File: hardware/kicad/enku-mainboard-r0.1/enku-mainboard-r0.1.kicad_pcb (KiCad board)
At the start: 4 copper layers, 54 x 94 mm, 124 parts, among them U1 ESP32-S3-WROOM-1-N16R8

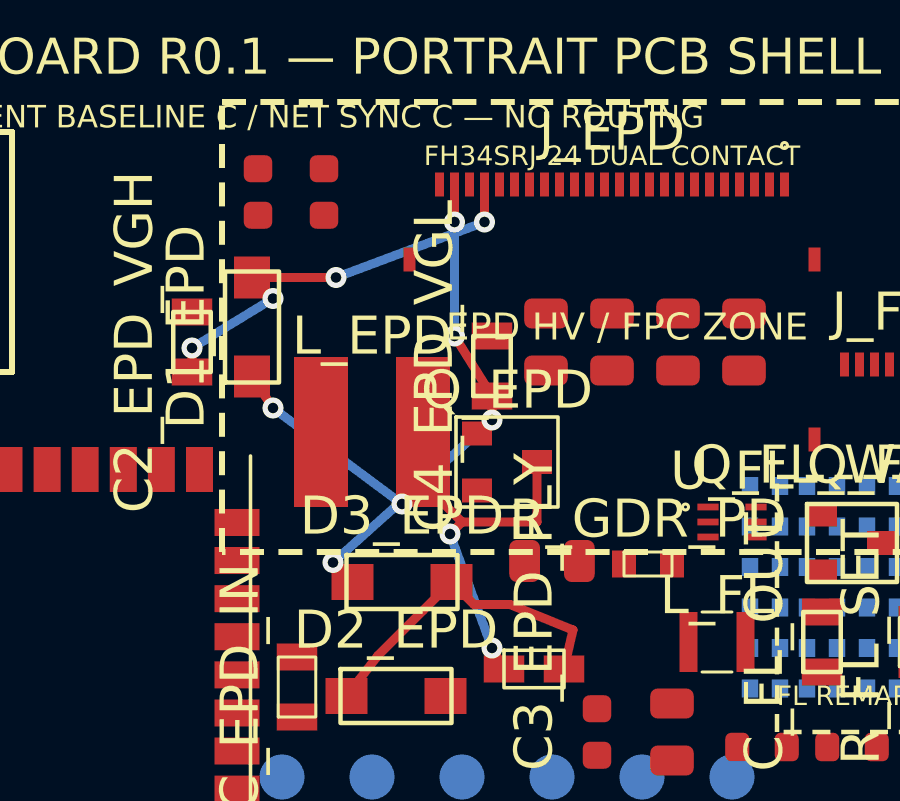
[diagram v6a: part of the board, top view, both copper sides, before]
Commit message: Reroute EPD VGL around proven HV paths
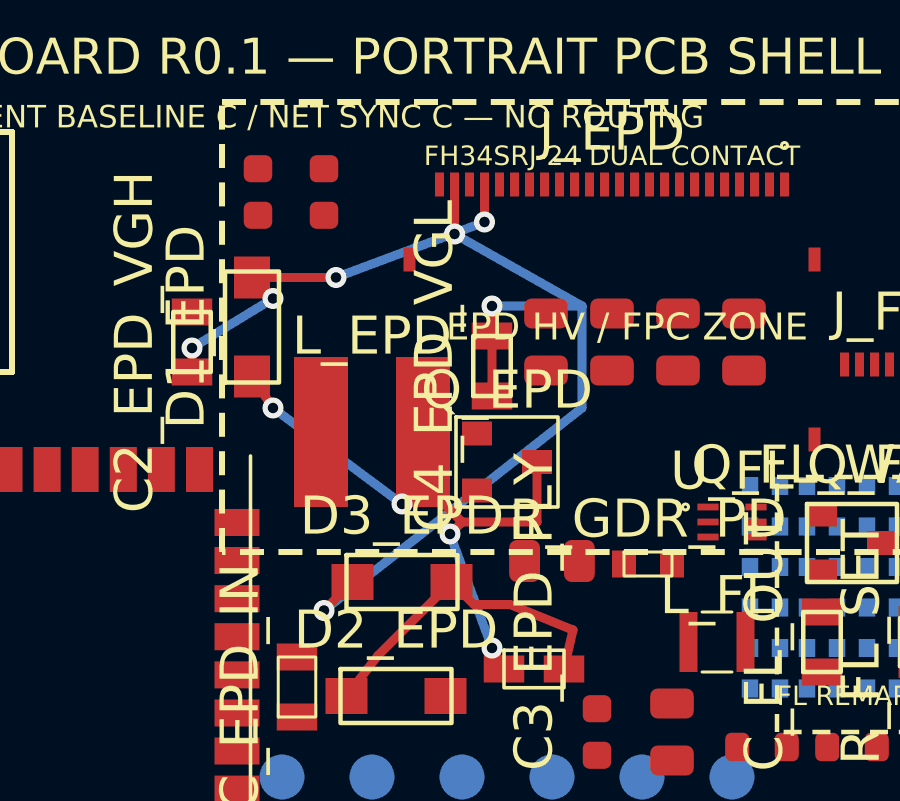
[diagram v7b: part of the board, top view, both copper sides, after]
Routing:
- net EPD_VGL: track 16.2 -> 28.2 mm, vias 4 -> 3
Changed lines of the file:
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@@
   (via (at 44.0 32.2) (size 0.7) (drill 0.35) (layers "F.Cu" "B.Cu") (net 26))
   (segment (start 44.0 32.2) (end 44.0 33.0) (width 0.3) (layer "F.Cu") (net 26))
-  (segment (start 49.35 40.0) (end 48.7 39.35) (width 0.3) (layer "F.Cu") (net 28))
-  (via (at 48.7 39.35) (size 0.7) (drill 0.35) (layers "F.Cu" "B.Cu") (net 28))
-  (segment (start 48.7 39.35) (end 54.0 34.6) (width 0.3) (layer "B.Cu") (net 28))
-  (via (at 54.0 34.6) (size 0.7) (drill 0.35) (layers "F.Cu" "B.Cu") (net 28))
-  (segment (start 54.0 34.6) (end 54.0 33.8) (width 0.3) (layer "F.Cu") (net 28))
-  (segment (start 54.0 33.8) (end 52.75 31.8) (width 0.3) (layer "F.Cu") (net 28))
-  (via (at 52.75 31.8) (size 0.7) (drill 0.35) (layers "F.Cu" "B.Cu") (net 28))
-  (segment (start 52.75 31.8) (end 52.75 28.0) (width 0.3) (layer "B.Cu") (net 28))
-  (via (at 52.75 28.0) (size 0.7) (drill 0.35) (layers "F.Cu" "B.Cu") (net 28))
-  (segment (start 52.75 28.0) (end 52.75 26.75) (width 0.3) (layer "F.Cu") (net 28))
+  (segment (start 49.35 40.0) (end 48.4 40.95) (width 0.3) (layer "F.Cu") (net 28))
+  (via (at 48.4 40.95) (size 0.7) (drill 0.35) (layers "F.Cu" "B.Cu") (net 28))
+  (segment (start 48.4 40.95) (end 57.0 34.2) (width 0.3) (layer "B.Cu") (net 28))
+  (segment (start 57.0 34.2) (end 57.0 30.8) (width 0.3) (layer "B.Cu") (net 28))
+  (segment (start 57.0 30.8) (end 54.0 30.8) (width 0.3) (layer "B.Cu") (net 28))
+  (via (at 54.0 30.8) (size 0.7) (drill 0.35) (layers "F.Cu" "B.Cu") (net 28))
+  (segment (start 54.0 30.8) (end 54.0 33.8) (width 0.3) (layer "F.Cu") (net 28))
+  (segment (start 57.0 30.8) (end 52.75 28.4) (width 0.3) (layer "B.Cu") (net 28))
+  (via (at 52.75 28.4) (size 0.7) (drill 0.35) (layers "F.Cu" "B.Cu") (net 28))
+  (segment (start 52.75 28.4) (end 52.75 26.75) (width 0.3) (layer "F.Cu") (net 28))
 )

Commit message: Move EPD VGL transit to inner layer
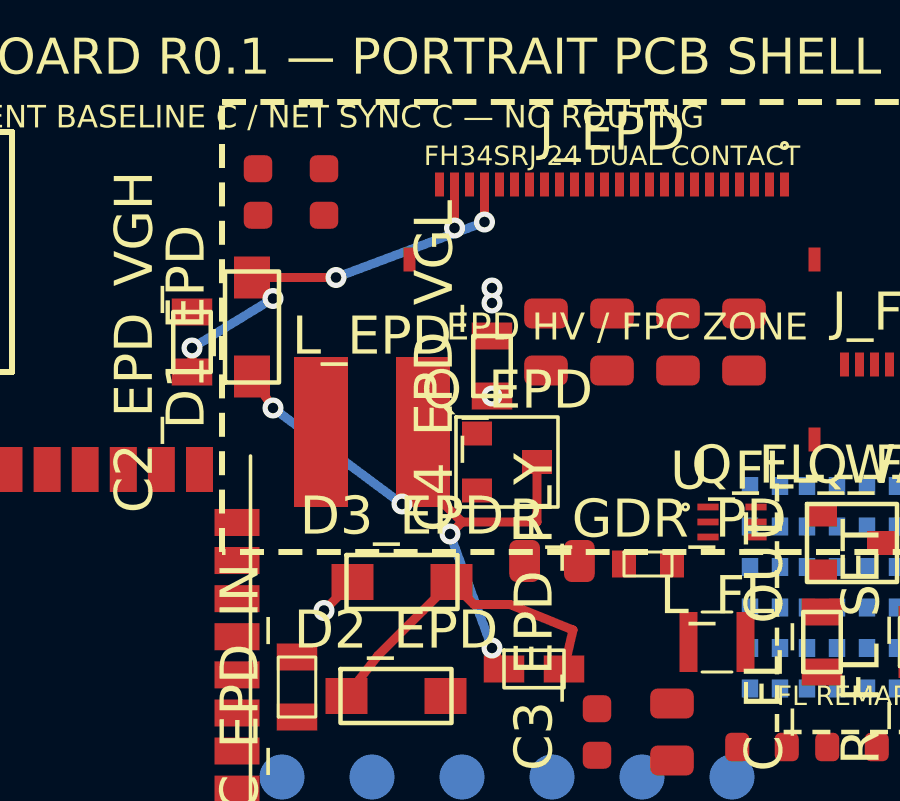
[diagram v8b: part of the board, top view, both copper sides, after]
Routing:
- net EPD_VGL: track 28.2 -> 28.6 mm, vias 3 -> 5
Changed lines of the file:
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@@
   (segment (start 44.0 32.2) (end 44.0 33.0) (width 0.3) (layer "F.Cu") (net 26))
   (segment (start 49.35 40.0) (end 48.4 40.95) (width 0.3) (layer "F.Cu") (net 28))
-  (via (at 48.4 40.95) (size 0.7) (drill 0.35) (layers "F.Cu" "B.Cu") (net 28))
-  (segment (start 48.4 40.95) (end 57.0 34.2) (width 0.3) (layer "B.Cu") (net 28))
-  (segment (start 57.0 34.2) (end 57.0 30.8) (width 0.3) (layer "B.Cu") (net 28))
-  (segment (start 57.0 30.8) (end 54.0 30.8) (width 0.3) (layer "B.Cu") (net 28))
-  (via (at 54.0 30.8) (size 0.7) (drill 0.35) (layers "F.Cu" "B.Cu") (net 28))
-  (segment (start 54.0 30.8) (end 54.0 33.8) (width 0.3) (layer "F.Cu") (net 28))
-  (segment (start 57.0 30.8) (end 52.75 28.4) (width 0.3) (layer "B.Cu") (net 28))
-  (via (at 52.75 28.4) (size 0.7) (drill 0.35) (layers "F.Cu" "B.Cu") (net 28))
-  (segment (start 52.75 28.4) (end 52.75 26.75) (width 0.3) (layer "F.Cu") (net 28))
+  (via (at 48.4 40.95) (size 0.7) (drill 0.35) (layers "F.Cu" "In1.Cu") (net 28))
+  (segment (start 48.4 40.95) (end 56.8 34.4) (width 0.3) (layer "In1.Cu") (net 28))
+  (segment (start 56.8 34.4) (end 56.8 30.2) (width 0.3) (layer "In1.Cu") (net 28))
+  (segment (start 56.8 30.2) (end 54.0 30.2) (width 0.3) (layer "In1.Cu") (net 28))
+  (via (at 54.0 30.2) (size 0.7) (drill 0.35) (layers "F.Cu" "In1.Cu") (net 28))
+  (segment (start 54.0 30.2) (end 54.0 30.7) (width 0.3) (layer "F.Cu") (net 28))
+  (via (at 54.0 30.7) (size 0.7) (drill 0.35) (layers "F.Cu" "In1.Cu") (net 28))
+  (segment (start 54.0 30.7) (end 54.0 33.8) (width 0.3) (layer "In1.Cu") (net 28))
+  (via (at 54.0 33.8) (size 0.7) (drill 0.35) (layers "F.Cu" "In1.Cu") (net 28))
+  (segment (start 56.8 30.2) (end 52.75 28.2) (width 0.3) (layer "In1.Cu") (net 28))
+  (via (at 52.75 28.2) (size 0.7) (drill 0.35) (layers "F.Cu" "In1.Cu") (net 28))
+  (segment (start 52.75 28.2) (end 52.75 26.75) (width 0.3) (layer "F.Cu") (net 28))
 )
